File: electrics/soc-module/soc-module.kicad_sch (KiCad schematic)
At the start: 19 parts, among them J1 Micro_SD, J2 East, J3 West, SW1 Prog, SW2 Reset, U1 ATECC608A-SSHDA, U2 ESP32-WROVER-IE-16MB

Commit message: Added product numbers for cost calculation
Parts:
- C1, C2, C3, C4: Price 0.08 -> (none); Product https://www.mouser.de/ProductDetail/KEMET/C1206C104M5RACTU?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 -> (none); manf# (none) -> C1206C104M5RACTU; mouser# (none) -> 80-C1206C104M5R
- J1: Price 2.19 -> (none); Product https://www.mouser.de/ProductDetail/Hirose-Connector/DM3AT-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 -> (none); manf# (none) -> MEM2061-01-188-00-A; mouser# (none) -> 640-MEM20610118800A
- J2, J3: Price 1.10 -> (none); Product https://www.mouser.de/ProductDetail/Samtec/TSW-114-08-T-S?q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 -> (none); manf# (none) -> 801-87-014-53-001101; mouser# (none) -> 437-8018701453001101
- R1, R2, R3, R4, R5, R6: Price 0.47 -> (none); Product https://www.mouser.de/ProductDetail/KOA-Speer/RN73H2BTTD100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 -> (none); manf# (none) -> CR0603AFX-1002EAS; mouser# (none) -> 652-CR0603AFX1002EAS
- SW1, SW2: Price 0.48 -> (none); Product https://www.mouser.de/ProductDetail/CK/KMR231NGLFS?qs=%2Fha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 -> (none)
- U1: Price 0.84 -> (none); Product https://www.mouser.de/ProductDetail/Microchip-Technology/AT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 -> (none); manf# (none) -> ATECC608A-SSHDA-B; mouser# (none) -> 556-ATECC608ASSHDAB
- U2: Price 3.26 -> (none); Product https://www.mouser.de/ProductDetail/Espressif-Systems/ESP32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 -> (none); manf# (none) -> ESP32-WROVER-IE-N16R8; mouser# (none) -> 356-ESP32WRVIE2864UC

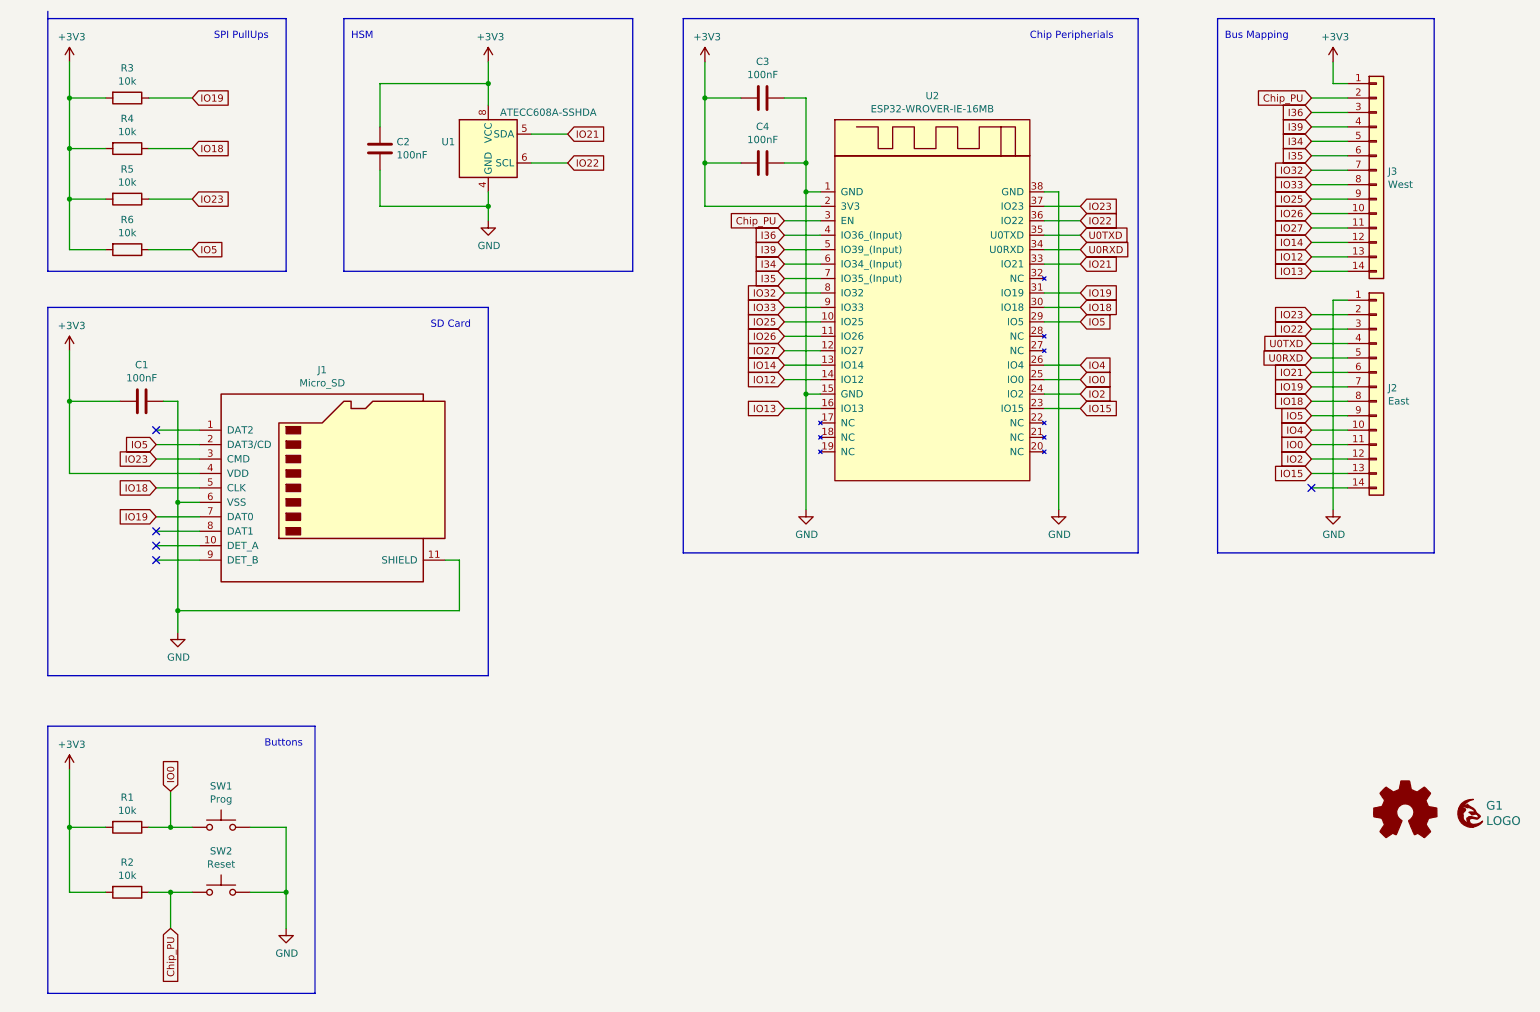
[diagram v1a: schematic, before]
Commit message: Feature/rtc for soc module (#10)
* Remove outdated files to clean things up

* Added missing part numbers for metering module

* Added 6 position screw terminal

* Added "mieterstrom" module

* Throw generated XML files out of version control

* Add "mieterstrom" module to local build

* Add "Mieterstrom" module to documentation

* Added "Mieterstrom" module to CI/CD

* Added optional RTC to SoC module
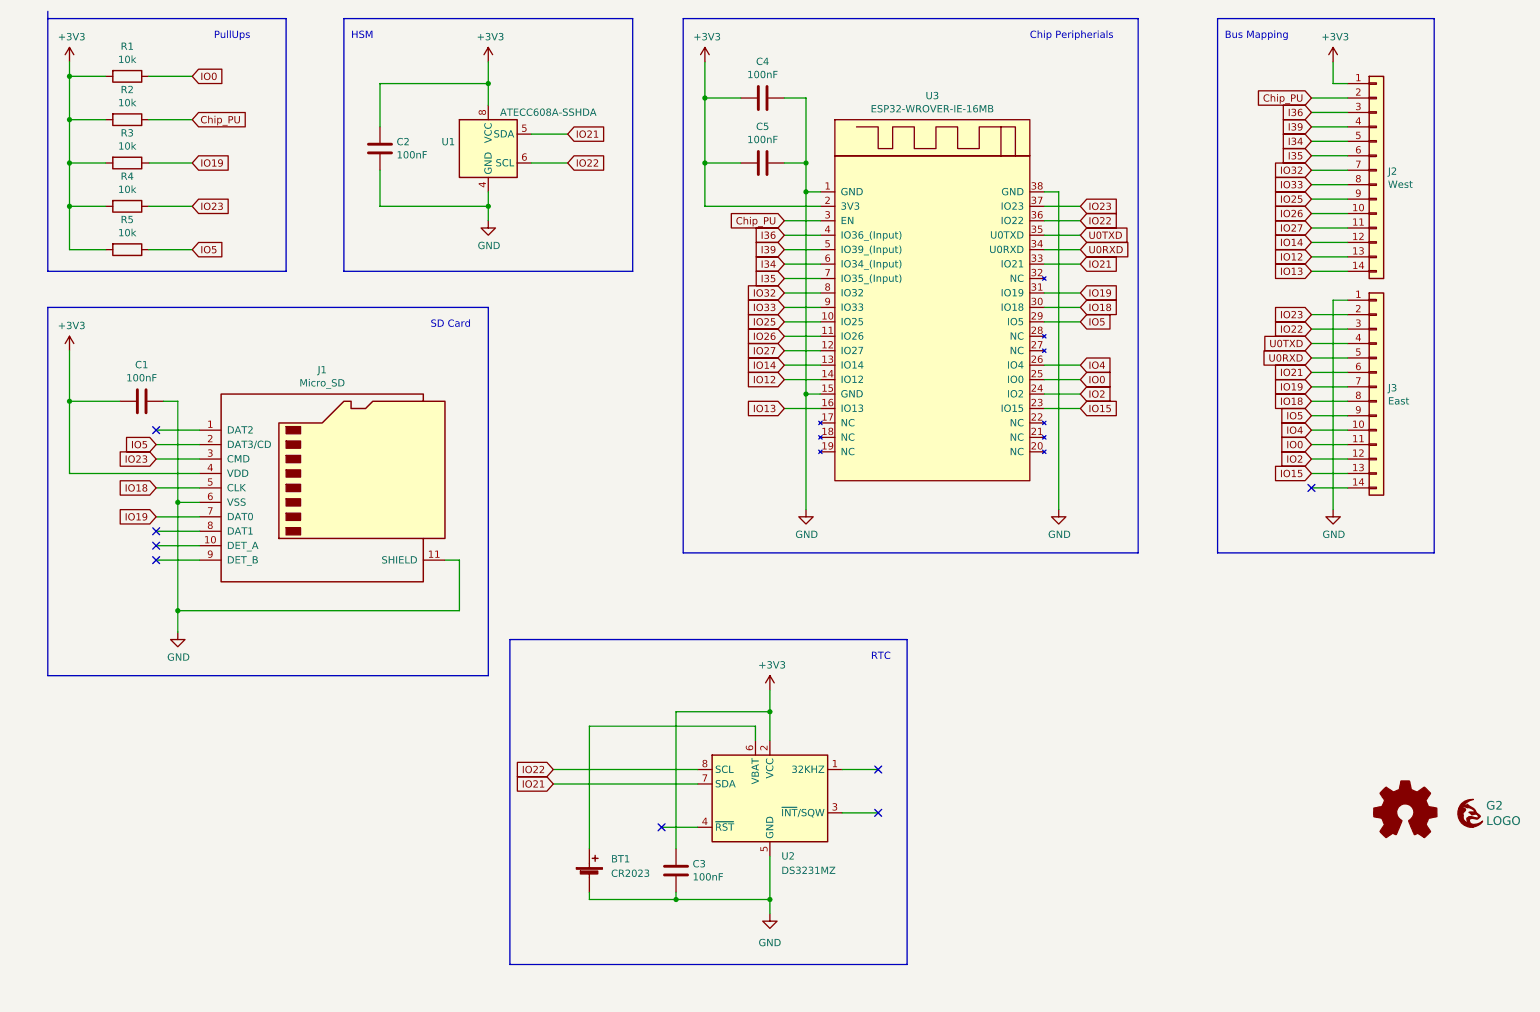
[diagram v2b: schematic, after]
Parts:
- removed R4: 10k, Resistor_SMD:R_1206_3216Metric_Pad1.30x1.75mm_HandSolder, symbol Device:R
- removed SW1: Prog, footprints:SW4SMD_63X161LS, symbol Switch:SW_Push
- removed SW2: Reset, footprints:SW4SMD_63X161LS, symbol Switch:SW_Push
- added BT1: CR2023, Battery:BatteryHolder_Keystone_1058_1x2032, symbol Device:Battery_Cell
- added C3: 100nF, Capacitor_SMD:C_1206_3216Metric_Pad1.33x1.80mm_HandSolder, symbol Device:C
- added U2: DS3231MZ, Package_SO:SOIC-8_3.9x4.9mm_P1.27mm, symbol Timer_RTC:DS3231MZ
- renumbered C3 to C4, C4 to C5, G2 to G1, G1 to G2, J3 to J2, J2 to J3, R5 to R4, R6 to R5, U2 to U3
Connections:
- net +3V3: now also C3.1, U2.2 (VCC)
- net GND: now also BT1.2 (-), C3.2, U2.5 (GND)
- net IO21: now also U2.7 (SDA)
- net IO22: now also U2.8 (SCL)
- new net: BT1.1 (+), U2.6 (VBAT)
- no-connect marks 5 -> 8
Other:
- note added: "PullUps"
- note added: "RTC"
- note removed: "Buttons"
- note removed: "SPI PullUps"
- moved on the sheet: R1, R2, R3, R4

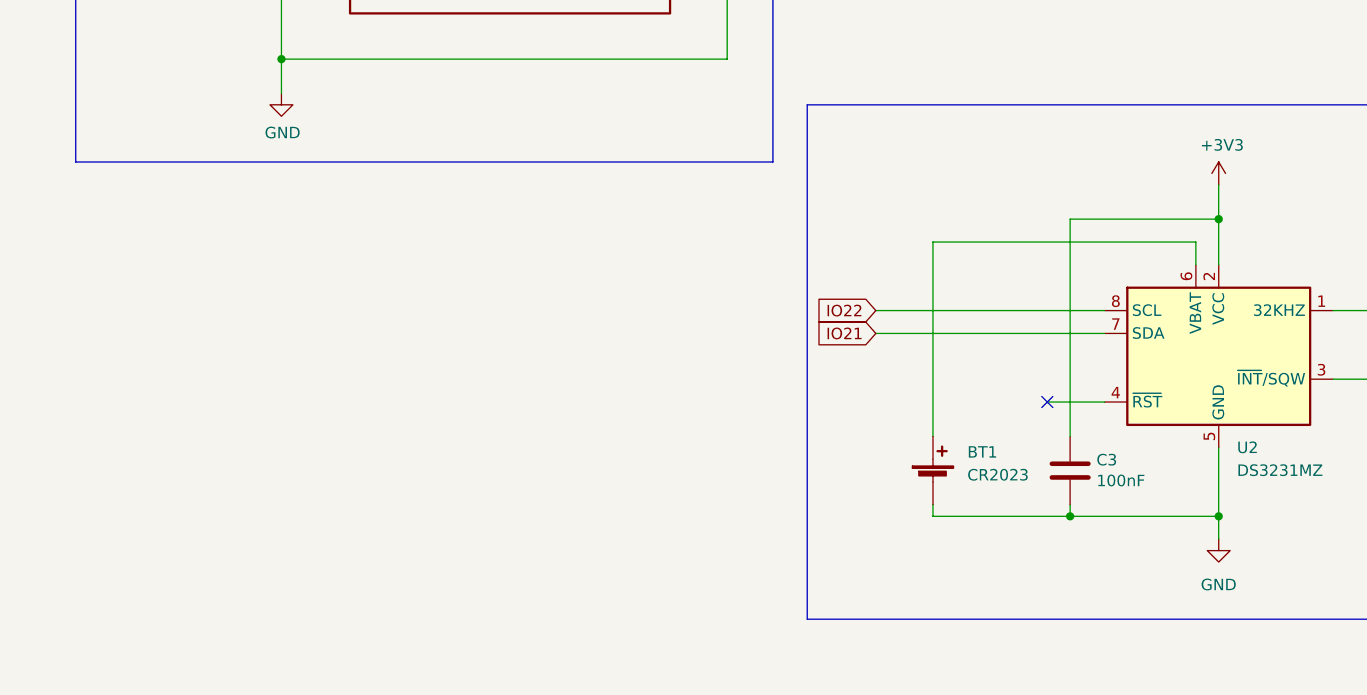
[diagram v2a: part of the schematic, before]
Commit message: Fix all ERC and DRC warnings during build
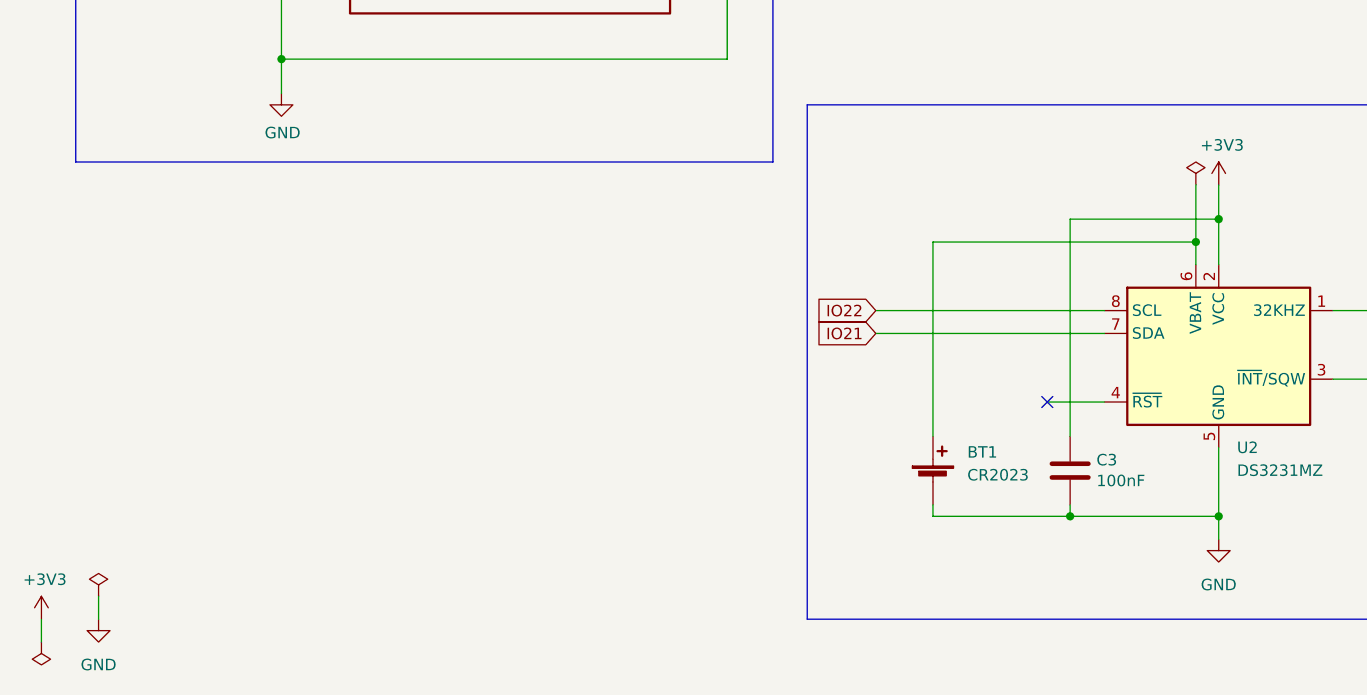
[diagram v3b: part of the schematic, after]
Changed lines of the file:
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@@
   (junction (at 45.72 124.46) (diameter 0) (color 0 0 0 0)
+  )
+  (junction (at 147.32 144.78) (diameter 0) (color 0 0 0 0)
   )
   (junction (at 133.35 175.26) (diameter 0) (color 0 0 0 0)
@@
     (stroke (width 0) (type default) (color 0 0 0 0))
   )
+  (wire (pts (xy 19.05 186.69) (xy 19.05 189.23))
+    (stroke (width 0) (type default) (color 0 0 0 0))
+  )
   (wire (pts (xy 200.66 106.68) (xy 200.66 50.8))
     (stroke (width 0) (type default) (color 0 0 0 0))
@@
     (stroke (width 0) (type default) (color 0 0 0 0))
   )
+  (wire (pts (xy 147.32 138.43) (xy 147.32 144.78))
+    (stroke (width 0) (type default) (color 0 0 0 0))
+  )
   (wire (pts (xy 26.67 53.34) (xy 26.67 60.96))
     (stroke (width 0) (type default) (color 0 0 0 0))
@@
   )
   (wire (pts (xy 41.91 95.25) (xy 49.53 95.25))
+    (stroke (width 0) (type default) (color 0 0 0 0))
+  )
+  (wire (pts (xy 25.4 184.15) (xy 25.4 186.69))
     (stroke (width 0) (type default) (color 0 0 0 0))
   )
@@
     )
   )
+  (symbol (lib_id "power:GND") (at 25.4 186.69 0) (unit 1)
+    (in_bom yes) (on_board yes) (fields_autoplaced)
+    (property "Reference" "#PWR0102" (id 0) (at 25.4 193.04 0)
+      (effects (font (size 1.27 1.27)) hide)
+    )
+    (property "Value" "GND" (id 1) (at 25.4 191.77 0))
+    (property "Footprint" "" (id 2) (at 25.4 186.69 0)
+      (effects (font (size 1.27 1.27)) hide)
+    )
+    (property "Datasheet" "" (id 3) (at 25.4 186.69 0)
+      (effects (font (size 1.27 1.27)) hide)
+    )
+    (pin "1")
+  )
+  (symbol (lib_id "power:+3V3") (at 19.05 186.69 0) (unit 1)
+    (in_bom yes) (on_board yes)
+    (property "Reference" "#PWR0101" (id 0) (at 19.05 190.5 0)
+      (effects (font (size 1.27 1.27)) hide)
+    )
+    (property "Value" "+3V3" (id 1) (at 19.431 182.2958 0))
+    (property "Footprint" "" (id 2) (at 19.05 186.69 0)
+      (effects (font (size 1.27 1.27)) hide)
+    )
+    (property "Datasheet" "" (id 3) (at 19.05 186.69 0)
+      (effects (font (size 1.27 1.27)) hide)
+    )
+    (pin "1")
+  )
+  (symbol (lib_id "power:PWR_FLAG") (at 19.05 189.23 180) (unit 1)
+    (in_bom yes) (on_board yes) (fields_autoplaced)
+    (property "Reference" "#FLG0101" (id 0) (at 19.05 191.135 0)
+      (effects (font (size 1.27 1.27)) hide)
+    )
+    (property "Value" "PWR_FLAG" (id 1) (at 19.05 194.31 0)
+      (effects (font (size 1.27 1.27)) hide)
+    )
+    (property "Footprint" "" (id 2) (at 19.05 189.23 0)
+      (effects (font (size 1.27 1.27)) hide)
+    )
+    (property "Datasheet" "~" (id 3) (at 19.05 189.23 0)
+      (effects (font (size 1.27 1.27)) hide)
+    )
+    (pin "1")
+  )
   (symbol (lib_id "Device:C") (at 133.35 170.18 0) (unit 1)
     (in_bom yes) (on_board yes)
@@
     (pin "2")
   )
+  (symbol (lib_id "power:PWR_FLAG") (at 25.4 184.15 0) (unit 1)
+    (in_bom yes) (on_board yes) (fields_autoplaced)
+    (property "Reference" "#FLG0102" (id 0) (at 25.4 182.245 0)
+      (effects (font (size 1.27 1.27)) hide)
+    )
+    (property "Value" "PWR_FLAG" (id 1) (at 25.4 179.07 0)
+      (effects (font (size 1.27 1.27)) hide)
+    )
+    (property "Footprint" "" (id 2) (at 25.4 184.15 0)
+      (effects (font (size 1.27 1.27)) hide)
+    )
+    (property "Datasheet" "~" (id 3) (at 25.4 184.15 0)
+      (effects (font (size 1.27 1.27)) hide)
+    )
+    (pin "1")
+  )
   (symbol (lib_id "power:+3V3") (at 149.86 138.43 0) (unit 1)
     (in_bom yes) (on_board yes)
@@
     )
     (property "Datasheet" "" (id 3) (at 149.86 138.43 0)
+      (effects (font (size 1.27 1.27)) hide)
+    )
+    (pin "1")
+  )
+  (symbol (lib_id "power:PWR_FLAG") (at 147.32 138.43 0) (unit 1)
+    (in_bom yes) (on_board yes) (fields_autoplaced)
+    (property "Reference" "#FLG0103" (id 0) (at 147.32 136.525 0)
+      (effects (font (size 1.27 1.27)) hide)
+    )
+    (property "Value" "PWR_FLAG" (id 1) (at 147.32 133.35 0)
+      (effects (font (size 1.27 1.27)) hide)
+    )
+    (property "Footprint" "" (id 2) (at 147.32 138.43 0)
+      (effects (font (size 1.27 1.27)) hide)
+    )
+    (property "Datasheet" "~" (id 3) (at 147.32 138.43 0)
       (effects (font (size 1.27 1.27)) hide)
     )
@@
   )
   (symbol_instances
+    (path "/6903d56f-74f5-4f2a-88ea-e29c9f5b6626"
+      (reference "#FLG0101") (unit 1) (value "PWR_FLAG") (footprint "")
+    )
+    (path "/98fd8a34-9f56-40d3-a160-8efea738e8b3"
+      (reference "#FLG0102") (unit 1) (value "PWR_FLAG") (footprint "")
+    )
+    (path "/e2a0839c-f67e-452d-ba55-52466f888f36"
+      (reference "#FLG0103") (unit 1) (value "PWR_FLAG") (footprint "")
+    )
     (path "/00000000-0000-0000-0000-000061986e9c"
       (reference "#PWR01") (unit 1) (value "+3V3") (footprint "")
@@
       (reference "#PWR012") (unit 1) (value "GND") (footprint "")
     )
+    (path "/270a12f2-49ef-4019-8dac-5e5b6b555acc"
+      (reference "#PWR0101") (unit 1) (value "+3V3") (footprint "")
+    )
+    (path "/1fc4ac31-c5c2-4205-ae19-4c4a902842a7"
+      (reference "#PWR0102") (unit 1) (value "GND") (footprint "")
+    )
     (path "/8d04db28-587f-40ce-88ca-5f8fa78962a8"
